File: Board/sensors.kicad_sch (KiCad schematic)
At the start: 19 parts, among them J7 TMP36GZ, U3 LM358, U5 LM358

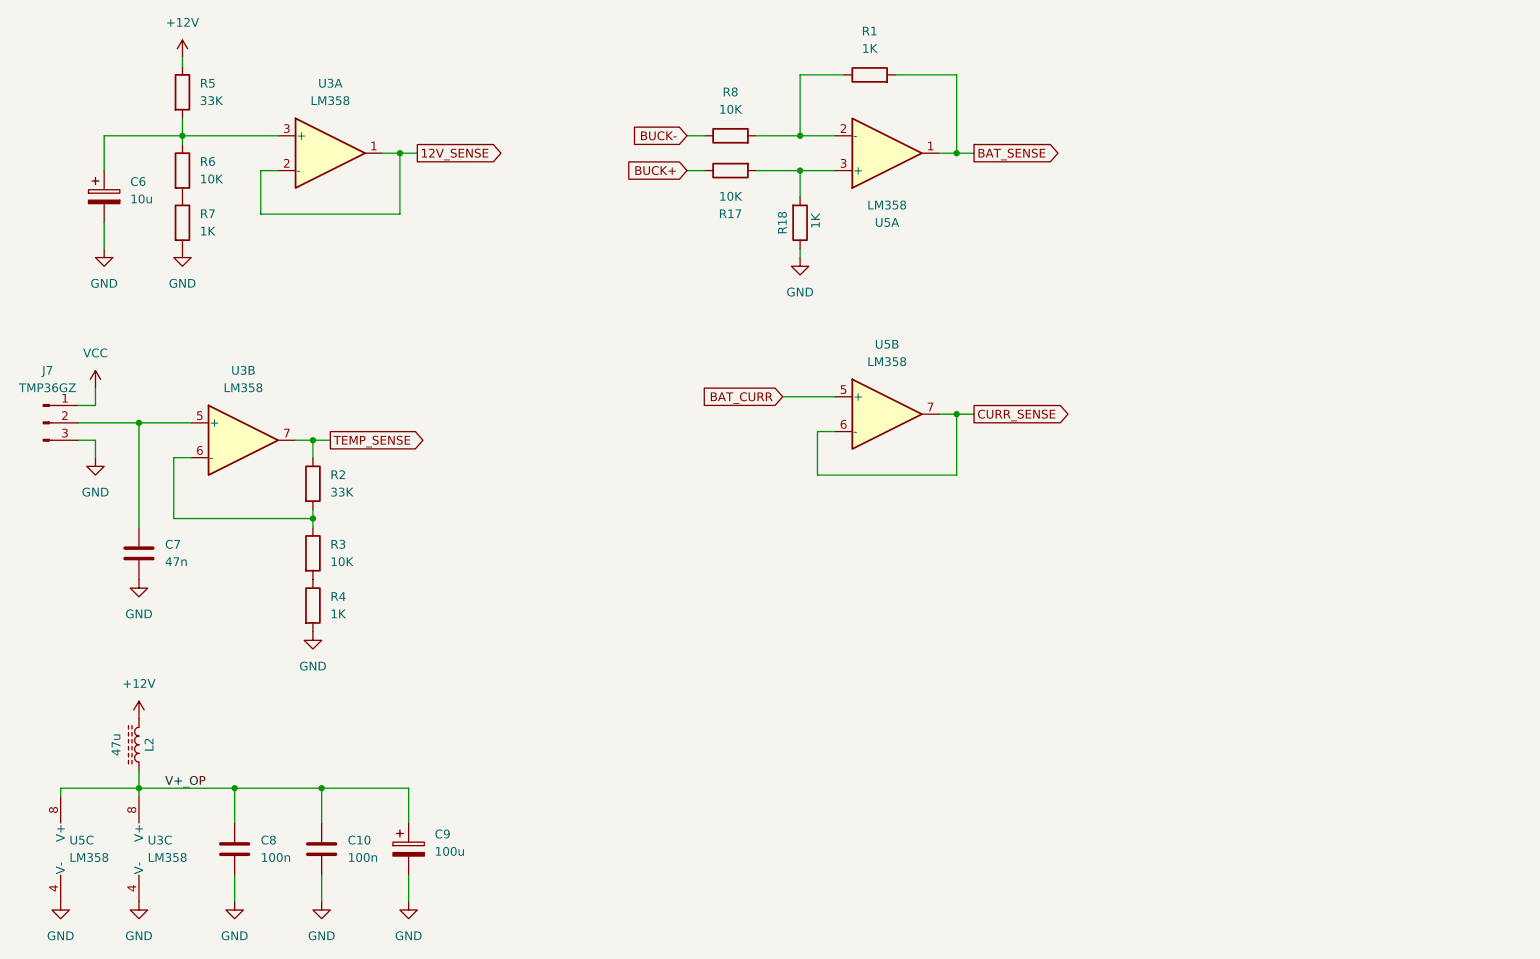
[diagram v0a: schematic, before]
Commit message: Fixes current sensor
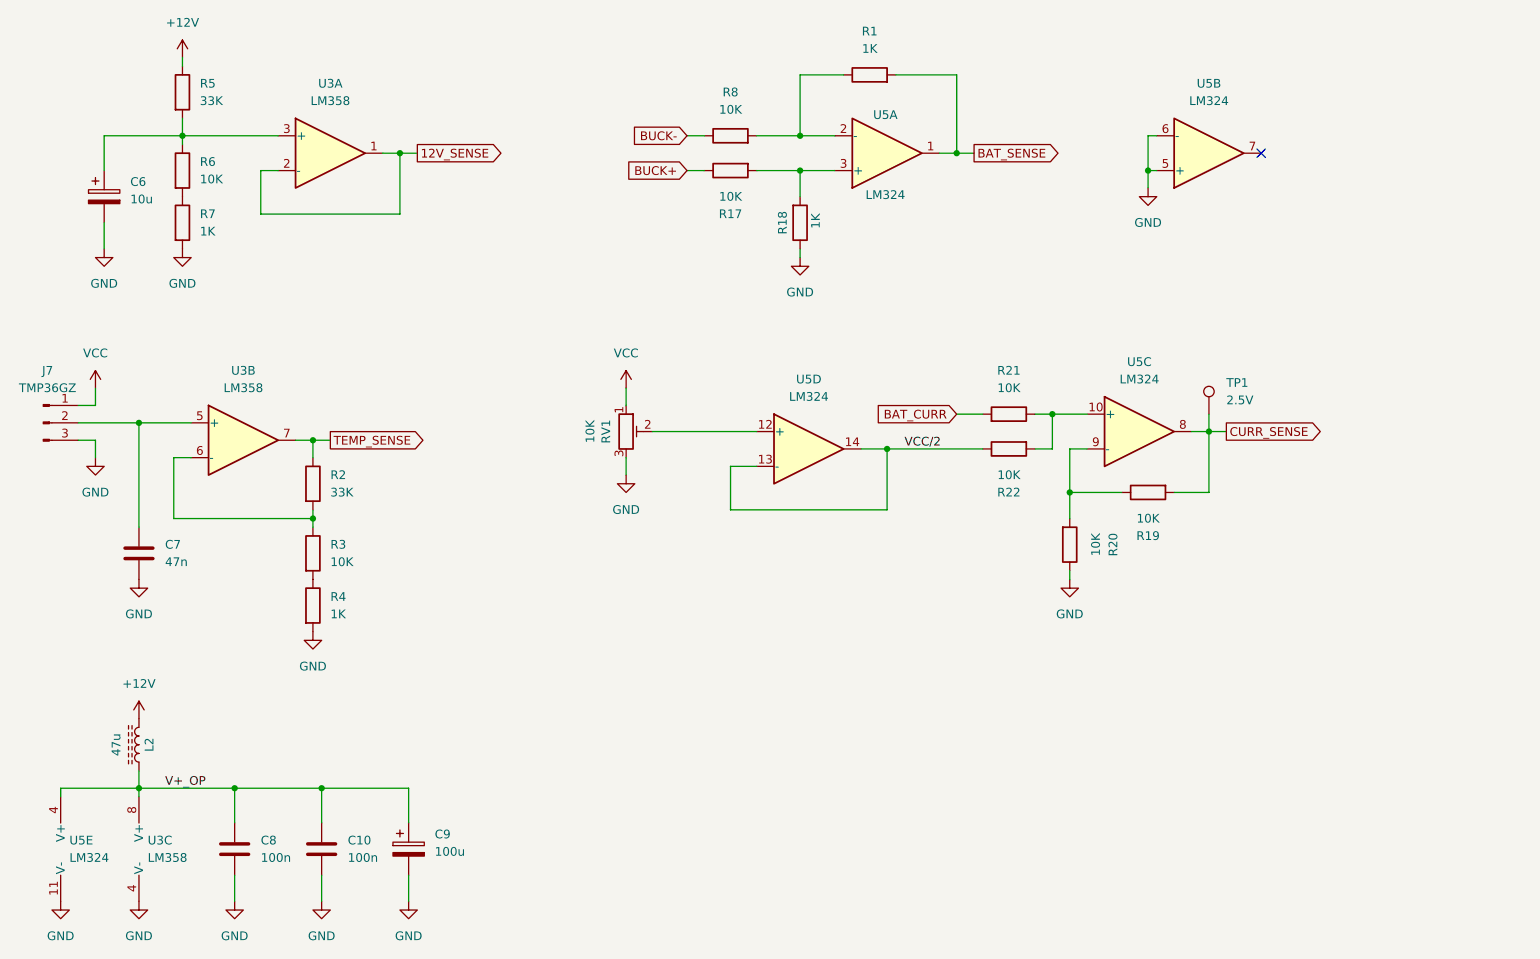
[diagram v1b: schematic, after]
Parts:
- removed U5: LM358, Package_SO:SOIC-8_3.9x4.9mm_P1.27mm, symbol Amplifier_Operational:LM358
- added R19, R20, R21, R22: 10K, Resistor_SMD:R_0805_2012Metric, symbol Device:R
- added RV1: 10K, Potentiometer_THT:Potentiometer_Bourns_3266Y_Vertical, symbol 64-ATX-rescue:R_POT_TRIM-Device
- added TP1: 2.5V, TestPoint:TestPoint_Loop_D1.80mm_Drill1.0mm_Beaded, symbol Connector:TestPoint
- added U5: LM324, Package_SO:SOIC-14_3.9x8.7mm_P1.27mm, symbol Amplifier_Operational:LM324
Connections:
- net BAT_CURR: now also R21.2
- net BAT_SENSE: now also U5.1
- net CURR_SENSE: now also R19.2, TP1.1, U5.8
- net GND: now also R20.1, RV1.3, U5.11 (V-), U5.5 (+), U5.6 (-)
- net V+_OP: now also U5.4 (V+)
- net VCC: now also RV1.1
- net at R1.1, R8.2: now also U5.2 (-)
- net at R17.2, R18.2: now also U5.3 (+)
- new net: R19.1, R20.2, U5.9 (-)
- new net: RV1.2, U5.12 (+)
- new net: R21.1, R22.2, U5.10 (+)
- new net VCC/2: R22.1, U5.13 (-), U5.14
- no-connect marks 0 -> 1

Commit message: Board WIP
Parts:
- C6: footprint Capacitor_SMD:CP_Elec_4x5.4 -> Capacitor_SMD:C_1206_3216Metric_Pad1.33x1.80mm_HandSolder
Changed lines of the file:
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@@
 			)
 		)
-		(property "Footprint" "Capacitor_SMD:CP_Elec_4x5.4"
+		(property "Footprint" "Capacitor_SMD:C_1206_3216Metric_Pad1.33x1.80mm_HandSolder"
 			(at 45.4152 53.34 0)
 			(effects

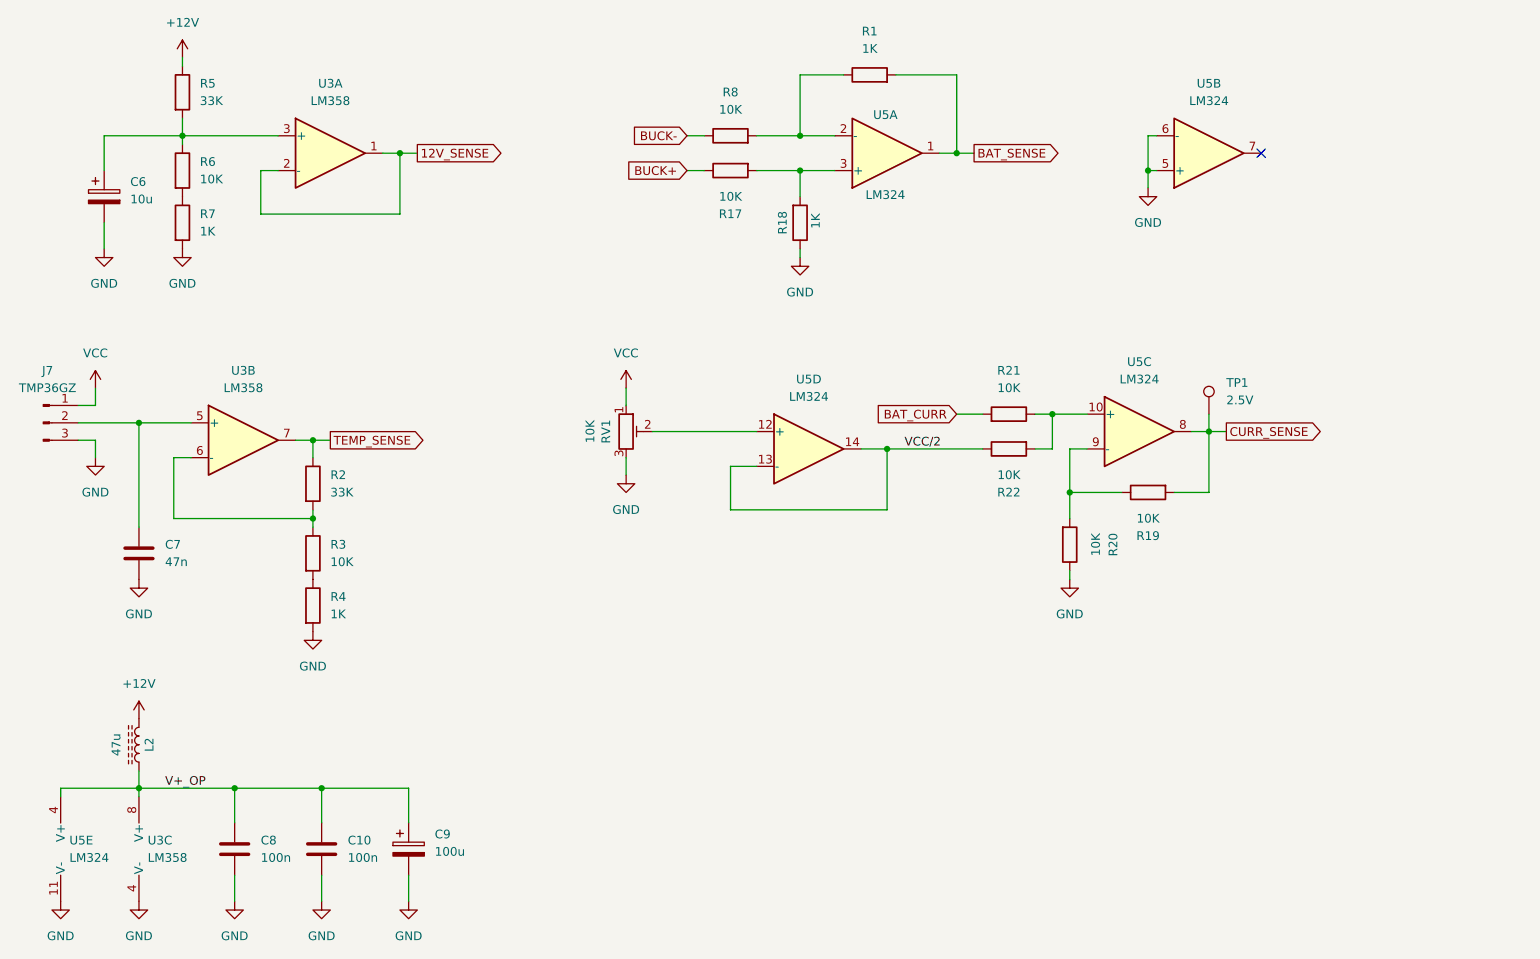
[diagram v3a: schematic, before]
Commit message: Schematic fixes
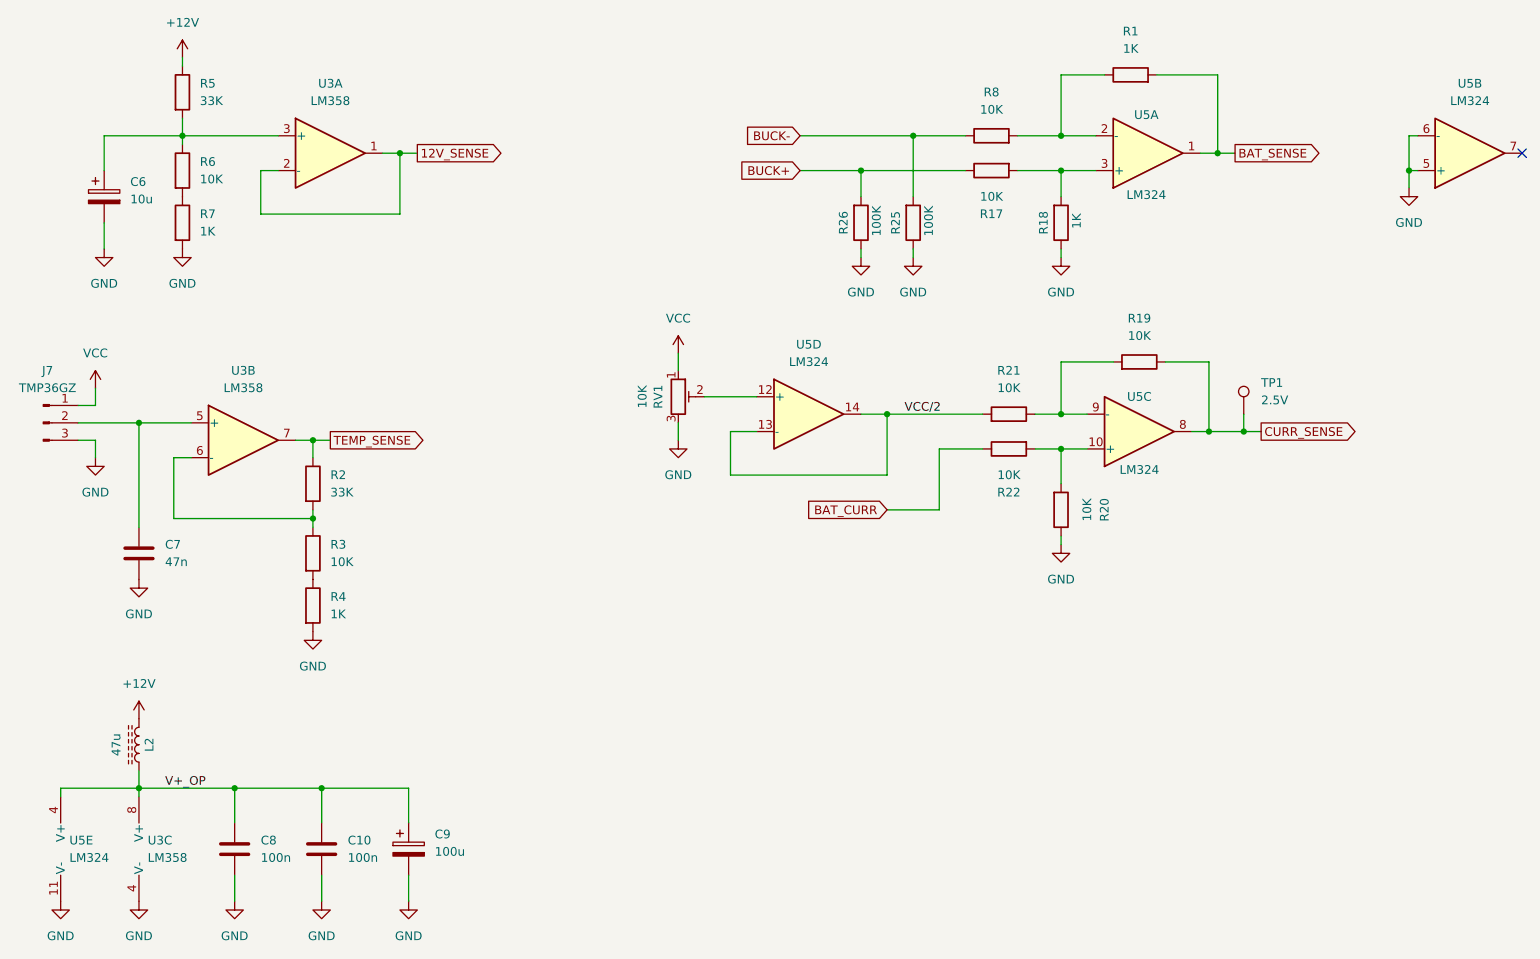
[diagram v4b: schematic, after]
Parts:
- added R25, R26: 100K, Resistor_SMD:R_0805_2012Metric, symbol Device:R
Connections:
- net BAT_CURR: now also R22.1; no longer R21.2
- net BUCK+: now also R26.2
- net BUCK-: now also R25.2
- net CURR_SENSE: now also R19.1; no longer R19.2
- net GND: now also R25.1, R26.1
- net VCC/2: now also R21.2; no longer R22.1
- net at R22.2, U5.10 (+): now also R20.2; no longer R21.1
- new net: R19.2, R21.1, U5.9 (-)
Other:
- moved on the sheet: R1, R17, R18, R19, R20, R8, RV1, TP1, U5A, U5B, U5D

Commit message: Fixes battery voltage sensing.
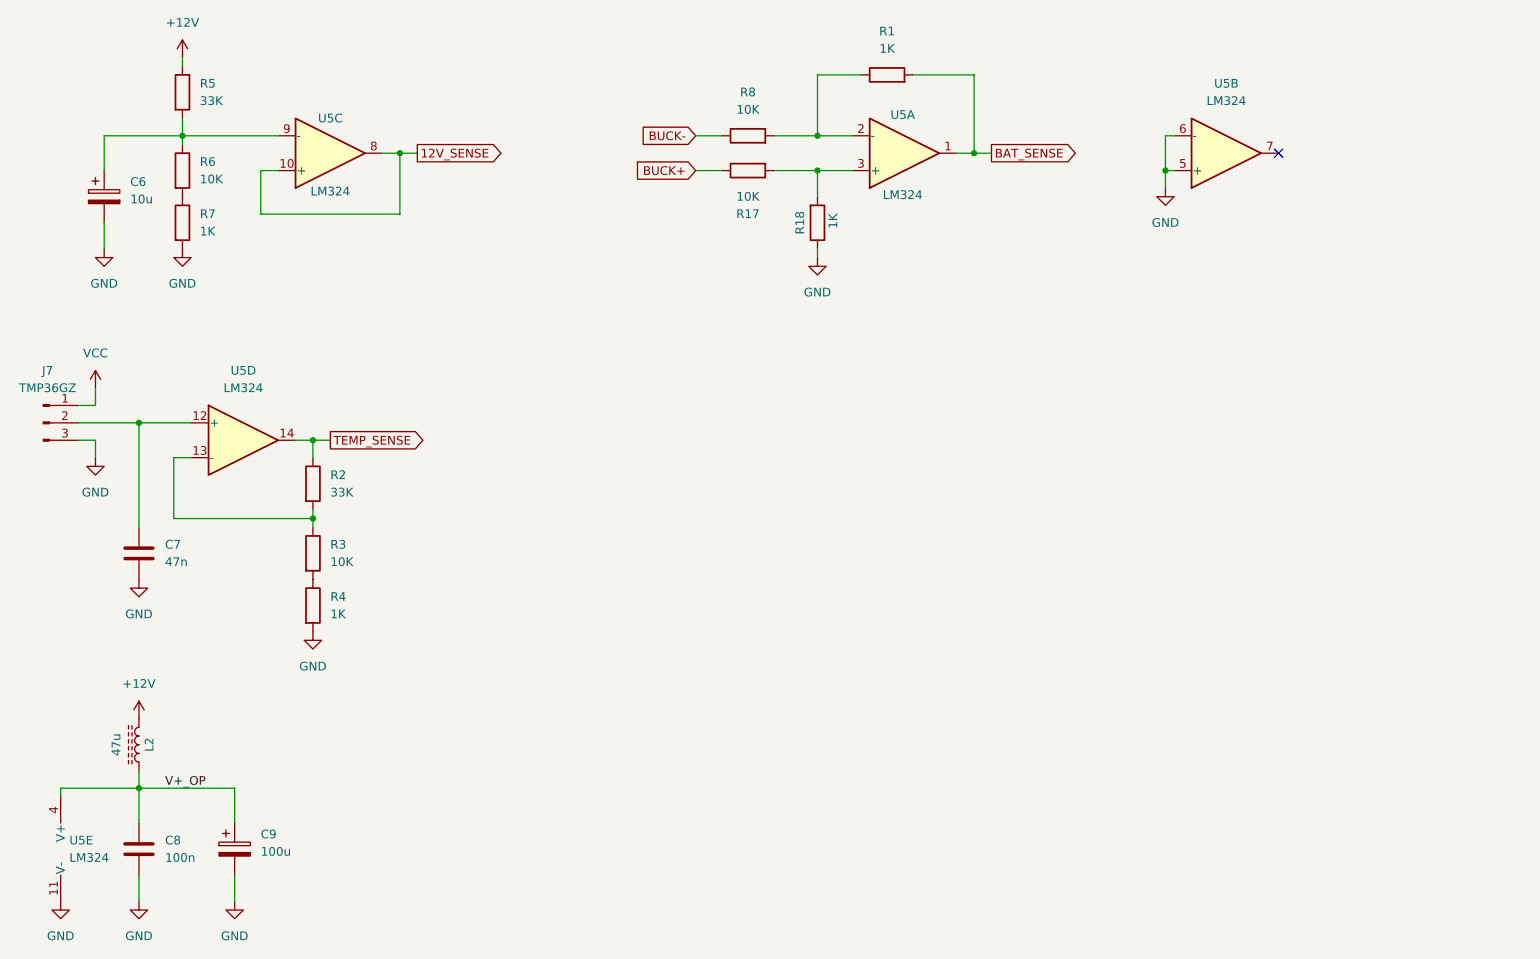
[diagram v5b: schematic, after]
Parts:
- removed C10: 100n, Capacitor_SMD:C_0805_2012Metric, symbol Device:C
- removed R19, R20, R21, R22: 10K, Resistor_SMD:R_0805_2012Metric, symbol Device:R
- removed R25, R26: 100K, Resistor_SMD:R_0805_2012Metric, symbol Device:R
- removed RV1: 10K, Potentiometer_THT:Potentiometer_Bourns_3266Y_Vertical, symbol 64-ATX-rescue:R_POT_TRIM-Device
- removed TP1: 2.5V, TestPoint:TestPoint_Loop_D1.80mm_Drill1.0mm_Beaded, symbol Connector:TestPoint
- removed U3: LM358, Package_SO:SOIC-8_3.9x4.9mm_P1.27mm, symbol Amplifier_Operational:LM358
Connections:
- net CURR_SENSE is gone; now on net 12V_SENSE: U5.8
- net 12V_SENSE: now also U5.10 (+)
- net TEMP_SENSE: now also U5.14
- net at C7.1, J7.2 (Pin_2): now also U5.12 (+)
- net at R2.2, R3.1: now also U5.13 (-)
- net at U5.9 (-): now also C6.1, R5.2, R6.1
- removed net VCC/2: U5.13 (-), U5.14
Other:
- moved on the sheet: C8, C9, R1, R17, R18, R8, U5A, U5B, U5C, U5D
